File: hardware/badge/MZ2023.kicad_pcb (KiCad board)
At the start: 2 copper layers, 77 x 51.3 mm, 59 parts, among them J1 Conn_01x04, J2 Conn_01x04, J3 Conn_01x04, J4 Conn_01x04, J5 Conn_01x08_Female, J6 Conn_01x02_Male, J7 Conn_01x07_Female, Q2 DMG2301L, SW1 SW_Push, SW2 SW_Push, SW3 SW_Push, SW4 SW_Push_SPDT, U1 Pico, U3 MCP73831-2-OT

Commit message: some parts anotated
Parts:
- removed D9: LED, LED_SMD:LED_1206_3216Metric_ReverseMount_Hole1.8x2.4mm
- added D8: LED, LED_SMD:LED_0603_1608Metric_Pad1.05x0.95mm_HandSolder, F.Cu at (169.7, 119.1)
- D10: value D -> LL4448 L1G

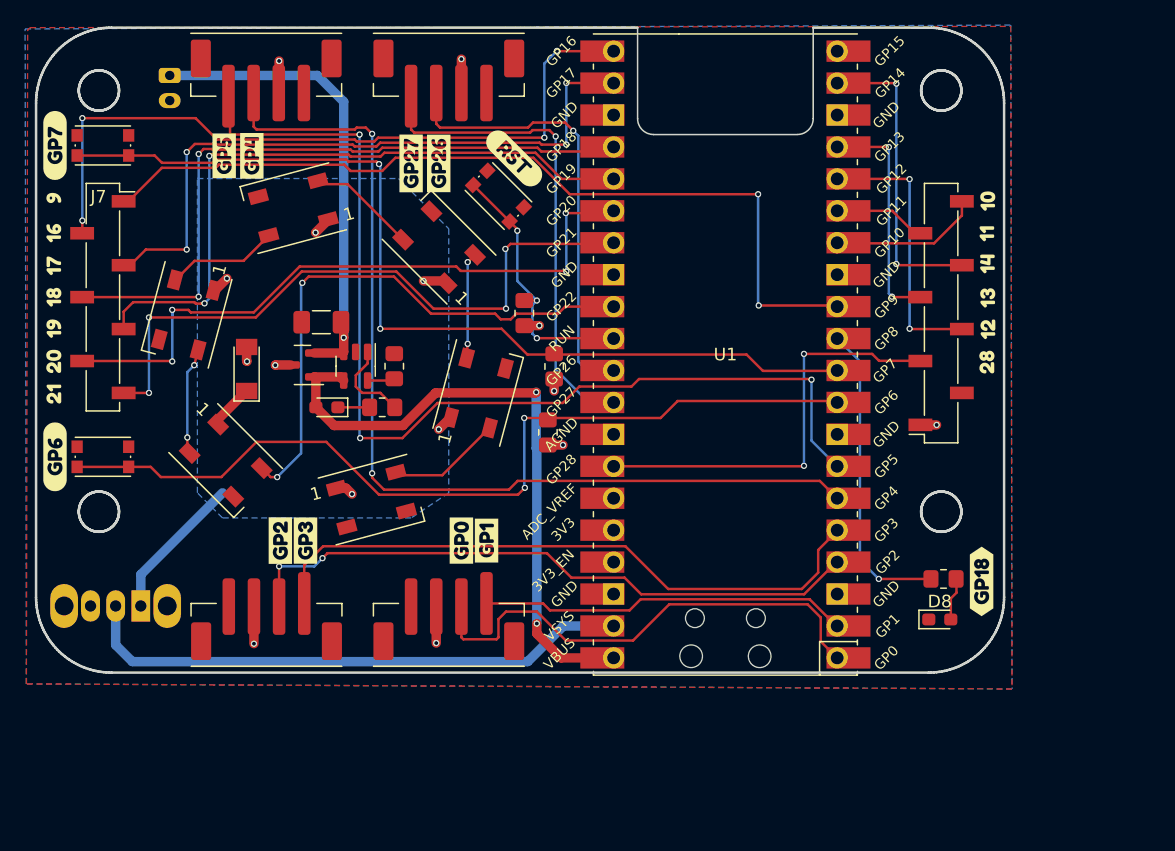
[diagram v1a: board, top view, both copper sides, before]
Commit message: new version: * added Seeed Studio LoRa e5 module * changed WS2812 LED from 5x5mm to 3.5x3.5mm footprint * changed WS2812 LED positions. From circle to "rectangular" with intention of becoming the top cover backlight * 2 Groove connectors (J3 and J4) removed from top and moved to bottom * Groove J4 connector now connected to GP20 and GP21 (previously GP4 and GP5) * Removed GP20 and GP21 from J7 pin header (the one on the left, 5 pins) * Added one extra GND and VCC pins to the connector J5 (the one on the right, 10 pins) * removed SW2 * SW4 (ON/OFF) moved on top * WS2812 takes power from VCC (either 5V from USB or the battery voltage * MCP73831 prog current set to 500mAh, fixed LED charging status
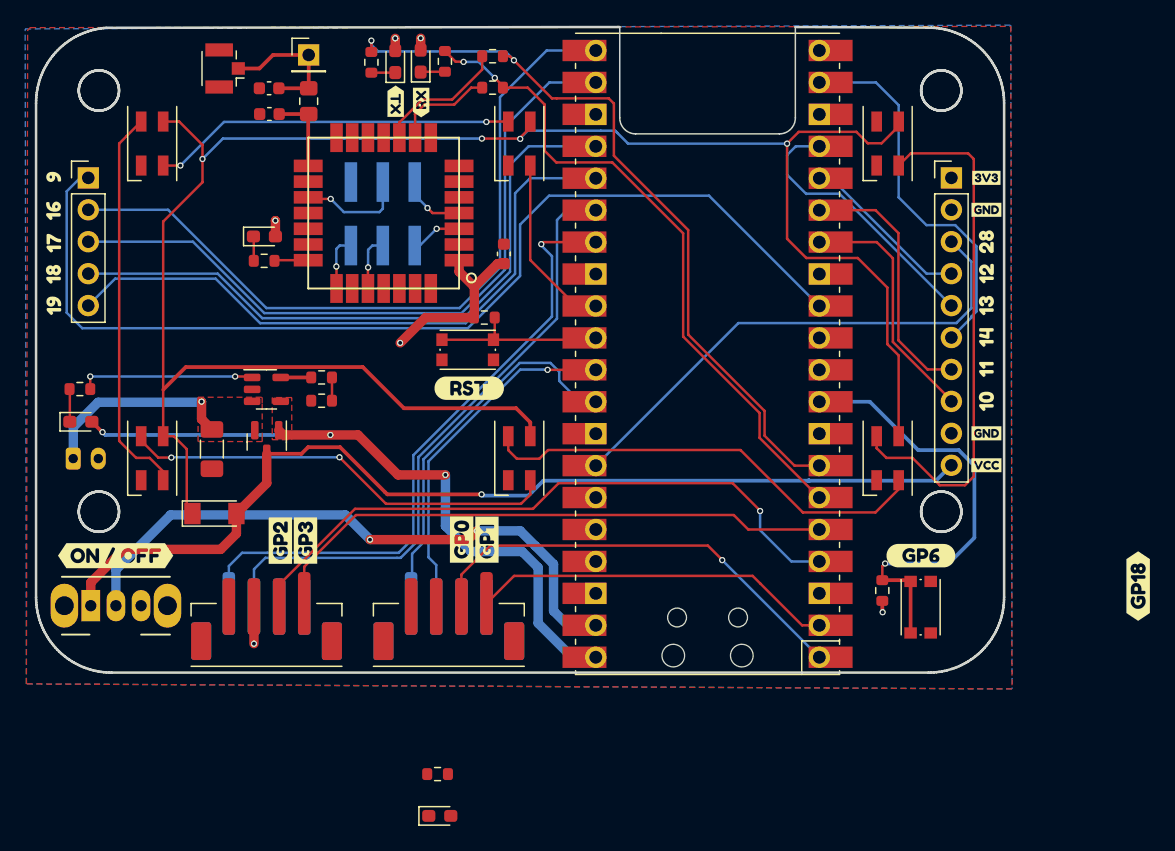
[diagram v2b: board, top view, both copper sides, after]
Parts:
- removed R2: 10k, Resistor_SMD:R_0805_2012Metric_Pad1.20x1.40mm_HandSolder
- removed SW2: SW_Push, Button_Switch_SMD:SW_Push_1P1T_NO_CK_KMR2
- removed kibuzzard-6368F1D8: G***, kibuzzard-6368F1D8
- removed kibuzzard-6368F201: G***, kibuzzard-6368F201
- removed kibuzzard-6370DC33: G***, kibuzzard-6370DC33
- removed kibuzzard-6370DC3A: G***, kibuzzard-6370DC3A
- removed kibuzzard-6370DC53: G***, kibuzzard-6370DC53
- removed kibuzzard-6370DC69: G***, kibuzzard-6370DC69
- removed kibuzzard-6370DCD1: G***, kibuzzard-6370DCD1
- removed kibuzzard-637FAC13: G***, kibuzzard-637FAC13
- removed kibuzzard-637FAC1E: G***, kibuzzard-637FAC1E
- added C1: 4.7u, Capacitor_SMD:C_0603_1608Metric, F.Cu at (135.0, 90.0)
- added C2: DNP, Capacitor_SMD:C_0603_1608Metric, F.Cu at (116.3, 78.9)
- added C4: DNP, Capacitor_SMD:C_0603_1608Metric, F.Cu at (116.3, 76.9)
- added D11: LED, LED_SMD:LED_0603_1608Metric_Pad1.05x0.95mm_HandSolder, F.Cu at (126.4, 74.8)
- added D12: LED, LED_SMD:LED_0603_1608Metric_Pad1.05x0.95mm_HandSolder, F.Cu at (128.4, 74.7)
- added D9: LED, LED_SMD:LED_0603_1608Metric_Pad1.05x0.95mm_HandSolder, F.Cu at (116.0, 88.7)
- added J8: Conn_Coaxial, Connector_Coaxial:U.FL_Hirose_U.FL-R-SMT-1_Vertical, F.Cu at (112.8, 75.3)
- added J9: Conn_02x03_Counter_Clockwise, Connector_PinHeader_2.54mm:PinHeader_2x03_P2.54mm_Vertical_SMD, B.Cu at (125.4, 86.9)
- added L1: 0, Inductor_SMD:L_0805_2012Metric_Pad1.15x1.40mm_HandSolder, F.Cu at (119.5, 77.9)
- added R10: 1k, Resistor_SMD:R_0603_1608Metric, F.Cu at (120.5, 101.7)
- added R11: 1k, Resistor_SMD:R_0603_1608Metric, F.Cu at (124.5, 74.8)
- added R12: 1k, Resistor_SMD:R_0603_1608Metric, F.Cu at (130.3, 74.7)
- added R7: 22, Resistor_SMD:R_0603_1608Metric, F.Cu at (134.1, 76.8)
- added R8: 22, Resistor_SMD:R_0603_1608Metric, F.Cu at (134.1, 74.3)
- added R9: 1k, Resistor_SMD:R_0603_1608Metric, F.Cu at (115.9, 90.6)
- added TP1: TestPoint, Connector_PinHeader_2.54mm:PinHeader_1x01_P2.54mm_Vertical, F.Cu at (119.5, 74.2)
- added U2: LoRa-E5, LoRa-E5:LoRa-E5, F.Cu at (125.4, 86.8)
- added kibuzzard-64457602: G***, kibuzzard-64457602, F.Cu at (133.7, 112.8)
- added kibuzzard-6445C087: G***, kibuzzard-6445C087, F.Cu at (126.4, 77.9)
- added kibuzzard-6445C08E: G***, kibuzzard-6445C08E, F.Cu at (128.4, 78.0)
- added kibuzzard-6445C19F: G***, kibuzzard-6445C19F, F.Cu at (168.2, 114.0)
- added kibuzzard-6445C37B: G***, kibuzzard-6445C37B, F.Cu at (173.4, 104.3)
- added kibuzzard-6445C37B: G***, kibuzzard-6445C37B, F.Cu at (173.4, 86.5)
- added kibuzzard-6445C3D4: G***, kibuzzard-6445C3D4, F.Cu at (173.4, 106.9)
- added kibuzzard-6445C3F3: G***, kibuzzard-6445C3F3, F.Cu at (173.4, 84.0)
- added kibuzzard-6445C7AF: G***, kibuzzard-6445C7AF, B.Cu at (115.2, 112.1)
- added kibuzzard-6445C7B7: G***, kibuzzard-6445C7B7, B.Cu at (113.1, 112.1)
- added kibuzzard-6445C7DF: G***, kibuzzard-6445C7DF, B.Cu at (127.6, 112.1)
- added kibuzzard-6445C7E9: G***, kibuzzard-6445C7E9, B.Cu at (129.7, 112.1)
- D1, D2, D3, D4, D5, D6: footprint LED_SMD:LED_WS2812B_PLCC4_5.0x5.0mm_P3.2mm -> LED_SMD:LED_SK6812MINI_PLCC4_3.5x3.5mm_P1.75mm
- J3, J4: moved to B.Cu
- J5: value Conn_01x08_Female -> Conn_01x10_Female; footprint Connector_PinSocket_2.54mm:PinSocket_1x08_P2.54mm_Vertical_SMD_Pin1Right -> Connector_PinHeader_2.54mm:PinHeader_1x10_P2.54mm_Vertical
- J7: value Conn_01x07_Female -> Conn_01x05_Female; footprint Connector_PinSocket_2.54mm:PinSocket_1x07_P2.54mm_Vertical_SMD_Pin1Right -> Connector_PinHeader_2.54mm:PinHeader_1x05_P2.54mm_Vertical
- R1, R4, R5, R6: footprint Resistor_SMD:R_0805_2012Metric_Pad1.20x1.40mm_HandSolder -> Resistor_SMD:R_0603_1608Metric
- R3: value 10k -> 1k; footprint Resistor_SMD:R_0805_2012Metric_Pad1.20x1.40mm_HandSolder -> Resistor_SMD:R_0603_1608Metric
- SW4, kibuzzard-636923C0: moved to F.Cu
- moved SW1 66.1 mm to (168.2, 118.2), turned to 90 degrees
- moved D6 49.9 mm to (165.5, 81.3), turned to -90 degrees
- moved J4 46.4 mm to (116.1, 120.9)
- moved J3 46.3 mm to (130.6, 120.9)
- moved R3 43.1 mm to (129.7, 131.4)
- moved D8 42.7 mm to (129.9, 134.8)
- moved D1 34.4 mm to (136.2, 81.3), turned to -90 degrees
- moved kibuzzard-6369234D 33.5 mm to (100.8, 108.4)
- moved D5 33.0 mm to (165.5, 106.3), turned to -90 degrees
- moved J6 31.4 mm to (100.7, 106.3), turned to 0 degrees
- moved kibuzzard-63692365 30.3 mm to (102.8, 108.2), turned to 180 degrees
- moved R1 29.4 mm to (165.1, 116.8)
- moved R6 24.1 mm to (101.3, 100.8), turned to 180 degrees
- moved D3 22.8 mm to (107.0, 106.3), turned to -90 degrees
- moved D7 19.6 mm to (101.3, 103.4), turned to 0 degrees
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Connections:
- net Net-(SW4-Pad2) renamed /VSYS
- D1 pad 1: Net-(D1-Pad1) -> Net-(D1-VDD)
- D10 pad 1: Net-(D1-Pad1) -> Net-(D1-VDD)
- D2 pad 1: VCC -> Net-(D1-VDD)
- D3 pad 1: VCC -> Net-(D1-VDD)
- D4 pad 1: VCC -> Net-(D1-VDD)
- D5 pad 1: VCC -> Net-(D1-VDD)
- D6 pad 1: VCC -> Net-(D1-VDD)
- D7 pad 1: Net-(D7-Pad1) -> Net-(D7-K)
- J4 pad 1: /GP5 -> /GP21
- J4 pad 2: /GP4 -> /GP20
- R5 pad 2: GND -> Net-(R10-Pad1)
- R6 pad 1: Net-(D7-Pad1) -> Net-(U3-STAT)
- R6 pad 2: Net-(R6-Pad2) -> Net-(D7-K)
- U3 pad 1: Net-(R6-Pad2) -> Net-(U3-STAT)
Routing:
- net Net-(D1-VDD): track 0.00 -> 158.4 mm, vias 0 -> 4
- net /GP7: track 75.4 -> 0.00 mm, vias 2 -> 0
- net VCC: track 21.5 -> 79.7 mm, vias 7 -> 1
- net /GP6: track 70.1 -> 36.3 mm, vias 2 -> 1
- net Net-(D5-DOUT): track 9.10 -> 42.0 mm
- net /NPXL: track 44.6 -> 14.2 mm, vias 2 -> 0
- net Net-(D4-DOUT): track 8.46 -> 36.3 mm, vias 2 -> 0
- net Net-(D3-DOUT): track 8.72 -> 34.9 mm, vias 0 -> 2
- net /GP4: track 78.1 -> 52.7 mm
- net /GP8: track 24.6 -> 0.00 mm, vias 1 -> 0
- net /GP5: track 83.2 -> 60.2 mm, vias 3 -> 2
- net Net-(D2-DOUT): track 8.90 -> 31.3 mm
- net +BATT: track 38.3 -> 16.1 mm
- net Net-(D1-DOUT): track 8.55 -> 28.9 mm
- net /GP9: track 68.7 -> 82.6 mm, vias 2 -> 0
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- added copper zone on F.Cu, net +BATT
- added copper zone on F.Cu, net VBUS
- removed copper zone on B.Cu, net VCC
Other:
- board size 77 x 51.3 mm -> 77 x 51.4 mm

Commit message: lora e5 v0.2 * changed grove connectors to right angle version * changed footprint for RDB LEDs WS2812B -> SK6812MINI (compatible with NeoPixels * mechanical switch (SW4) now cut the BAT+ instead of VCC (VSYS) * move lipo charging circuit to free space for new grove connectors and MKZH logo * created MakeZurich logo * improved silk
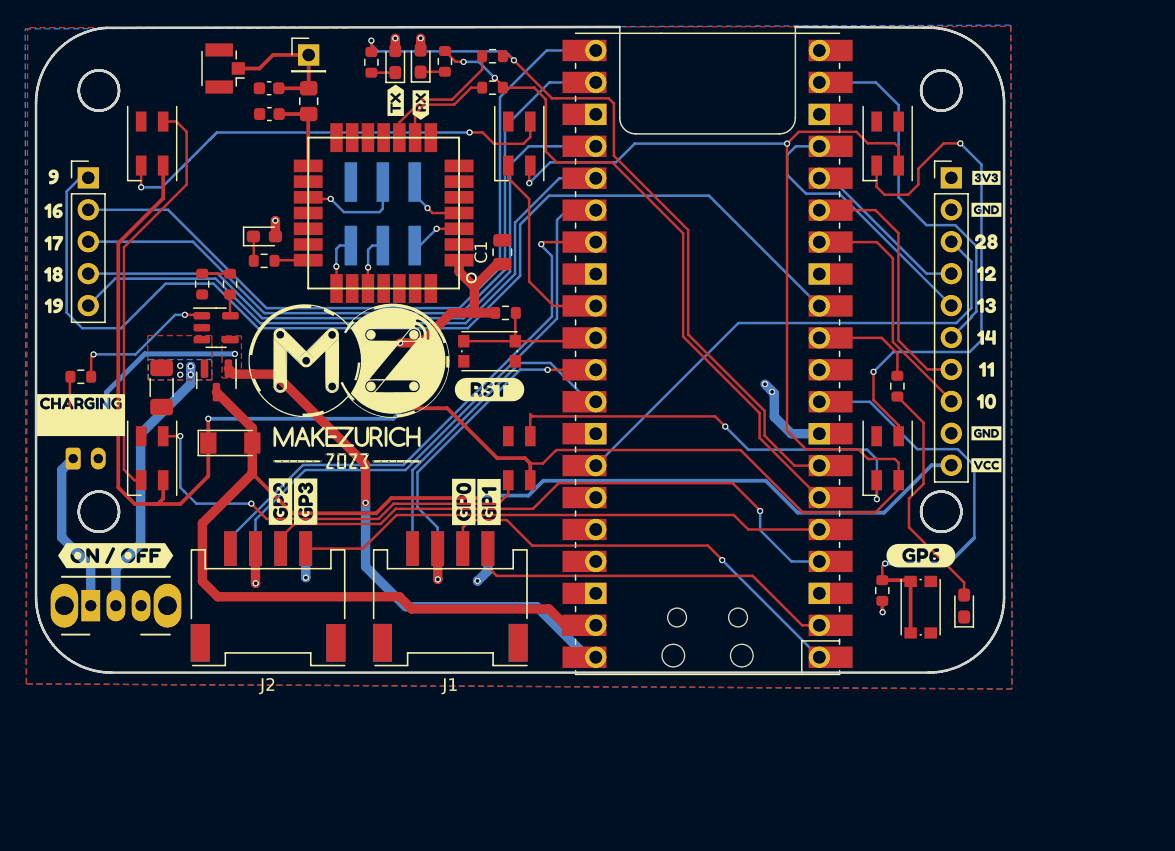
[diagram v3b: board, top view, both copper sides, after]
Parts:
- removed kibuzzard-6370DCFF: G***, kibuzzard-6370DCFF
- removed kibuzzard-6445C087: G***, kibuzzard-6445C087
- added G***: LOGO, LOGO, F.Cu at (122.7, 100.6)
- added REF**: MountingHole_3.2mm_M3, MountingHole:MountingHole_3.2mm_M3, F.Cu at (102.8, 110.6)
- added REF**: MountingHole_3.2mm_M3, MountingHole:MountingHole_3.2mm_M3, F.Cu at (102.8, 77.1)
- added REF**: MountingHole_3.2mm_M3, MountingHole:MountingHole_3.2mm_M3, F.Cu at (169.8, 110.5)
- added REF**: MountingHole_3.2mm_M3, MountingHole:MountingHole_3.2mm_M3, F.Cu at (169.8, 77.1)
- added REF**: KiCad-Logo2_5mm_SilkScreen, Symbol:KiCad-Logo2_5mm_SilkScreen, B.Cu at (109.0, 89.1)
- added REF**: OSHW-Logo2_7.3x6mm_SilkScreen, Symbol:OSHW-Logo2_7.3x6mm_SilkScreen, B.Cu at (168.0, 117.8)
- added kibuzzard-64484314: G***, kibuzzard-64484314, F.Cu at (126.4, 77.8)
- added kibuzzard-64568B8C: G***, kibuzzard-64568B8C, B.Cu at (127.9, 93.5)
- added kibuzzard-64568C60: G***, kibuzzard-64568C60, B.Cu at (125.4, 93.5)
- added kibuzzard-64568EFC: G***, kibuzzard-64568EFC, B.Cu at (125.4, 80.2)
- added kibuzzard-64568F15: G***, kibuzzard-64568F15, B.Cu at (127.9, 80.2)
- added kibuzzard-645D57F9: G***, kibuzzard-645D57F9, F.Cu at (101.3, 102.9)
- C1: footprint Capacitor_SMD:C_0603_1608Metric -> Capacitor_SMD:C_0805_2012Metric
- D1, D2, D3, D4, D5, D6: value WS2812B -> SK6812MINI
- J1, J2, J3, J4: footprint Tillo:Grove_SMD -> OPL_Connector:HW4-SMD-2.0-90D
- moved R3 47.9 mm to (166.3, 100.6), turned to -90 degrees
- moved D8 44.9 mm to (171.6, 118.1), turned to 90 degrees
- moved R10 13.3 mm to (111.0, 92.5), turned to -90 degrees
- moved R5 10.4 mm to (113.2, 92.5), turned to 90 degrees
- moved C3 6.33 mm to (107.8, 100.7)
- moved Q2 6.33 mm to (112.1, 100.1)
- moved U3 6.33 mm to (112.1, 95.9)
- moved D10 5.75 mm to (113.2, 105.1)
- moved kibuzzard-6370DC90 3.10 mm to (117.2, 109.8)
- moved kibuzzard-6370DC98 3.10 mm to (119.2, 109.8)
- moved kibuzzard-6445C7AF 3.05 mm to (115.2, 109.0)
- moved kibuzzard-6445C7B7 3.05 mm to (113.2, 109.0)
- moved kibuzzard-6445C7DF 3.05 mm to (127.7, 109.1)
- moved kibuzzard-6445C7E9 3.05 mm to (129.7, 109.1)
- moved kibuzzard-64457602 2.99 mm to (133.8, 109.8)
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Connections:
- C3 pad 1: +BATT -> /VBAT
- D1 pad 1: Net-(D1-VDD) -> Net-(D1-DOUT)
- D1 pad 2: Net-(D1-DOUT) -> GND
- D1 pad 3: GND -> /NPXL
- D1 pad 4: /NPXL -> Net-(D1-VDD)
- D2 pad 1: Net-(D1-VDD) -> Net-(D2-DOUT)
- D2 pad 2: Net-(D2-DOUT) -> GND
- D2 pad 3: GND -> Net-(D1-DOUT)
- D2 pad 4: Net-(D1-DOUT) -> Net-(D1-VDD)
- D3 pad 1: Net-(D1-VDD) -> Net-(D3-DOUT)
- D3 pad 2: Net-(D3-DOUT) -> GND
- D3 pad 3: GND -> Net-(D2-DOUT)
- D3 pad 4: Net-(D2-DOUT) -> Net-(D1-VDD)
- D4 pad 1: Net-(D1-VDD) -> Net-(D4-DOUT)
- D4 pad 2: Net-(D4-DOUT) -> GND
- D4 pad 3: GND -> Net-(D3-DOUT)
- D4 pad 4: Net-(D3-DOUT) -> Net-(D1-VDD)
- D5 pad 1: Net-(D1-VDD) -> Net-(D5-DOUT)
- D5 pad 2: Net-(D5-DOUT) -> GND
- D5 pad 3: GND -> Net-(D4-DOUT)
- D5 pad 4: Net-(D4-DOUT) -> Net-(D1-VDD)
- D6 pad 1: Net-(D1-VDD) -> unconnected-(D6-DOUT-Pad1)
- D6 pad 2: unconnected-(D6-DOUT-Pad2) -> GND
- D6 pad 3: GND -> Net-(D5-DOUT)
- D6 pad 4: Net-(D5-DOUT) -> Net-(D1-VDD)
- Q2 pad 2: +BATT -> /VBAT
- SW4 pad 1: VCC -> +BATT
- SW4 pad 2: /VSYS -> /VBAT
- U1 pad 10: /GP7 -> unconnected-(U1-GPIO7-Pad10)
- U1 pad 20: /GP15 -> unconnected-(U1-GPIO15-Pad20)
- U1 pad 39: /VSYS -> VCC
- U3 pad 3: +BATT -> /VBAT
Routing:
- net /VSYS: track 49.2 -> 0.00 mm, vias 2 -> 0
- net VCC: track 79.7 -> 111.8 mm
- net /VBAT: track 0.00 -> 21.5 mm, vias 0 -> 4
- net Net-(D8-A): track 0.00 -> 18.9 mm
- net Net-(D1-VDD): track 158.4 -> 174.9 mm
- net GND: track 4.42 -> 16.7 mm, vias 1 -> 5
- net Net-(D1-DOUT): track 28.9 -> 37.8 mm
- net /GP8: track 0.00 -> 8.50 mm
- net /GP21: track 51.3 -> 44.2 mm
- net /GP20: track 50.5 -> 44.2 mm
- net /GP27: track 30.5 -> 25.6 mm
- net /GP26: track 28.2 -> 24.3 mm
- net /GP3: track 46.1 -> 42.4 mm
- net +3V3: track 22.1 -> 25.7 mm, vias 6 -> 7
- net +BATT: track 16.1 -> 13.0 mm, vias 1 -> 0
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- added copper zone on B.Cu, net /VBAT
- added copper zone on F.Cu, net /VBAT
- removed copper zone on F.Cu, net +BATT

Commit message: added GND under antenna, added teardrops
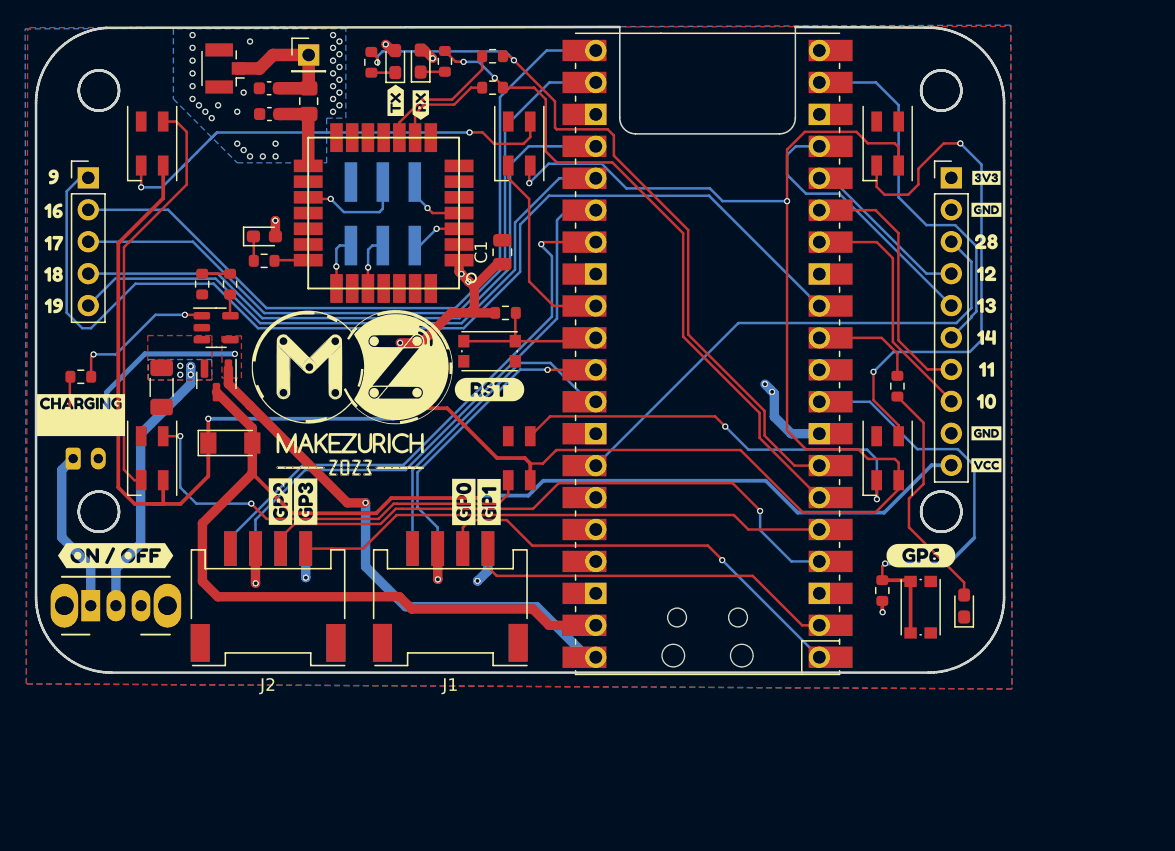
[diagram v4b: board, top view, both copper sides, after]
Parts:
- moved G*** 0.57 mm to (122.9, 101.1)
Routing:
- net Net-(D4-DOUT): track 35.5 -> 34.3 mm
- net VBUS: track 58.1 -> 57.0 mm
- net Net-(D1-VDD): track 174.9 -> 175.5 mm
- net /GP5: track 60.2 -> 59.7 mm
- net +3V3: track 25.7 -> 26.0 mm, vias 7 -> 9
- net GND: vias 5 -> 37
- added copper zone on B.Cu, net GND

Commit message: improvements to the LoRa antenna * changed the shape of the copper plane underneath the LoRa antenna path * moved D1-DOUT track on btm outside the antenna btm gnd plane
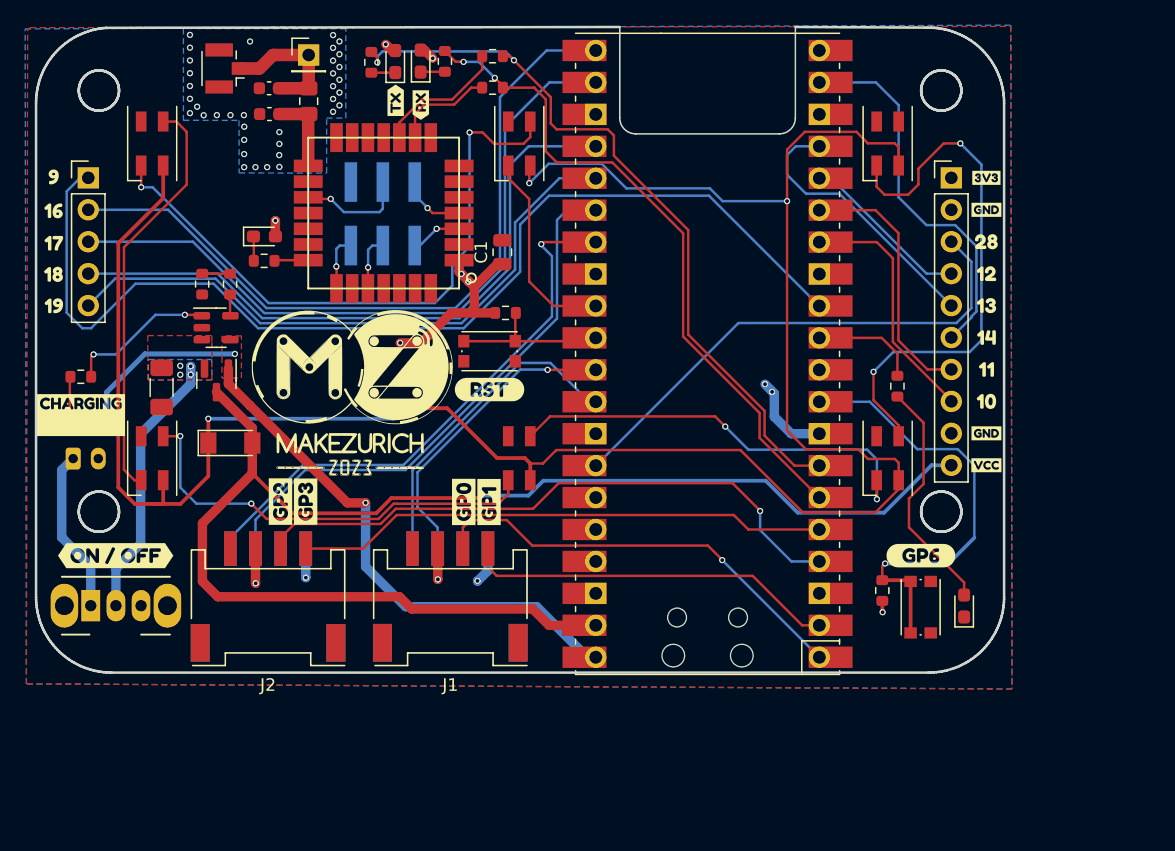
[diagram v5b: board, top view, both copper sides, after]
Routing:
- net Net-(D1-DOUT): track 37.8 -> 50.3 mm
- net GND: vias 37 -> 41
